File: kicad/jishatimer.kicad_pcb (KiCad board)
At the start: 2 copper layers, 48.3 x 39.3 mm, 13 parts

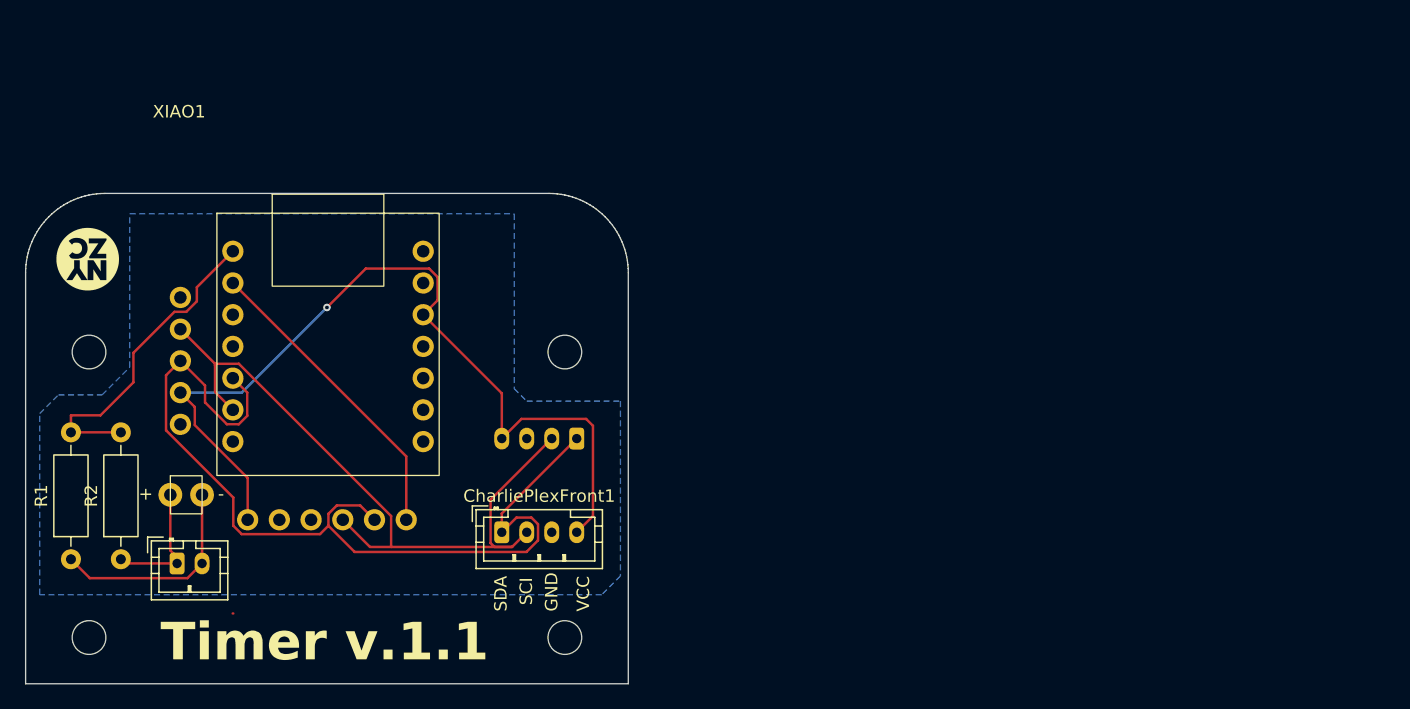
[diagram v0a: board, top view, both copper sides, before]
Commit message: Replace LED matrix displays with single SH1106 OLED
Swap the dual IS31FL3731 LED matrix setup for one SH1106 OLED driven
via U8g2, removing the orientation-based top/bottom display switching
that's no longer needed. Also make RTC and accelerometer init
failures non-fatal so the device stays usable with degraded hardware,
and add serial diagnostic commands (X: OLED probe, I: full I2C scan)
plus a matching hardware test suite check.

Ignore KiCad's auto-generated backup/history/lock files going forward.
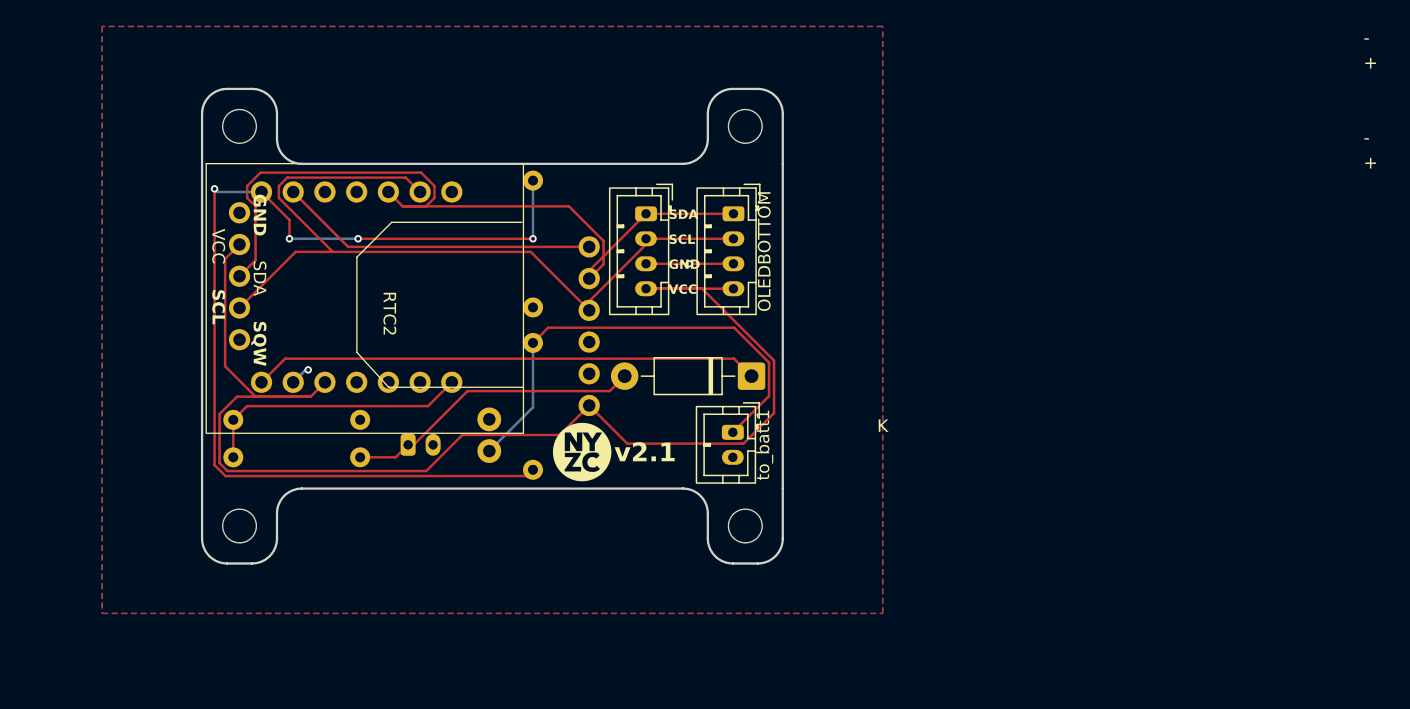
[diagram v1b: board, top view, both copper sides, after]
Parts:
- removed Accelerometer1: ~, Alex Library:Adafruit_LIS3DH
- removed CharliePlexBack1, CharliePlexFront1: ~, Connector_JST:JST_PH_B4B-PH-K_1x04_P2.00mm_Vertical
- removed REF**1, REF**2, REF**3: MountingHole_2.7mm, MountingHole:MountingHole_2.7mm
- removed RTC1: ~, Alex Library:Adafruit_ PCF8523
- added Accelerometer2: ~, Alex Library:Adafruit_LIS3DH, B.Cu at (152.0, 67.0)
- added Hole1: MountingHole_2.7mm, MountingHole:MountingHole_2.7mm, F.Cu at (117.5, 83.0)
- added Hole1: MountingHole_2.7mm, MountingHole:MountingHole_2.7mm, F.Cu at (117.5, 51.0)
- added Hole1: MountingHole_2.7mm, MountingHole:MountingHole_2.7mm, F.Cu at (158.0, 83.0)
- added OLEDBOTTOM1: ~, Connector_JST:JST_PH_B4B-PH-K_1x04_P2.00mm_Vertical, F.Cu at (157.1, 58.0)
- added OLEDTOP1: ~, Connector_JST:JST_PH_B4B-PH-K_1x04_P2.00mm_Vertical, F.Cu at (150.1, 58.0)
- added R3: R, Resistor_THT:R_Axial_DIN0207_L6.3mm_D2.5mm_P10.16mm_Horizontal, B.Cu at (117.0, 74.5)
- added R4: R, Resistor_THT:R_Axial_DIN0207_L6.3mm_D2.5mm_P10.16mm_Horizontal, B.Cu at (127.2, 77.5)
- added RTC2: ~, Alex Library:Adafruit_ PCF8523, F.Cu at (124.7, 65.9)
- added Schottky1: D_Schottky, Diode_THT:D_DO-41_SOD81_P10.16mm_Horizontal, F.Cu at (158.5, 71.0)
- added pogo1: ~, Connector_JST:JST_PH_B2B-PH-K_1x02_P2.00mm_Vertical, B.Cu at (131.0, 76.5)
- R1, R2, XIAO1, to_xiao1: moved to B.Cu
- moved to_batt1 45.7 mm to (157.0, 75.5), turned to -90 degrees
- moved Hole2 43.4 mm to (158.0, 51.0)
- moved R1 42.1 mm to (141.0, 65.5)
- moved R2 37.3 mm to (141.0, 68.3), turned to -90 degrees
- moved to_xiao1 20.9 mm to (131.2, 69.6), turned to 90 degrees
- moved XIAO1 1.79 mm to (114.2, 55.0), turned to -90 degrees
- renumbered REF** to Hole2
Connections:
- net Net-(to_batt1-+) renamed +BATT
- R1 pad 1: Net-(to_batt1--) -> GND
- XIAO1 pad 5V: unconnected-(XIAO1-VUSB-Pad5V) -> Net-(Schottky1-K)
- XIAO1 pad D2: Net-(XIAO1-A2) -> unconnected-(XIAO1-A2-PadD2)
- XIAO1 pad D7: unconnected-(XIAO1-PadD7) -> Net-(R3-Pad1)
- XIAO1 pad GND: Net-(Accelerometer1-PadGND) -> GND
- to_batt1 pad 2: Net-(to_batt1--) -> GND
- to_xiao1 pad -: Net-(to_batt1--) -> GND
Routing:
- net Net-(XIAO1-A0): track 25.8 -> 80.9 mm, vias 0 -> 4
- net Net-(Schottky1-K): track 0.00 -> 40.6 mm
- net Net-(OLEDBOTTOM1-VCC): track 70.7 -> 104.4 mm, vias 1 -> 0
- net +BATT: track 10.4 -> 37.5 mm
- net VCC: track 0.00 -> 23.9 mm
- net Net-(R3-Pad1): track 0.00 -> 21.7 mm
- net Net-(to_batt1--): track 17.1 -> 0.00 mm
- net Net-(OLEDBOTTOM1-SDA): track 74.4 -> 64.1 mm
- net GND: track 0.00 -> 8.61 mm, vias 0 -> 2
- net Net-(OLEDBOTTOM1-SCL): track 58.2 -> 65.5 mm
- net Net-(XIAO1-A1): track 24.7 -> 25.5 mm
- added copper zone on B.Cu, net GND
- added copper zone on F.Cu, net GND
- removed copper zone on B.Cu, net Net-(Accelerometer1-PadGND)
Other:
- board size 48.3 x 39.3 mm -> 46.5 x 38 mm
- board text added: "+"
- board text added: "-"
- board text added: "GND"
- board text added: "SCL"
- board text added: "SDA"
- board text added: "VCC"
- board text added: "v2.1"
- board text removed: "Timer v.1.1"
